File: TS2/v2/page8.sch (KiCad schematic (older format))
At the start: 16 parts, among them SW4 ABORT, U28 74LS148, U32 74LS138, U33 74LS138, U34 74LS00, U35 74LS74, U4 74LS06

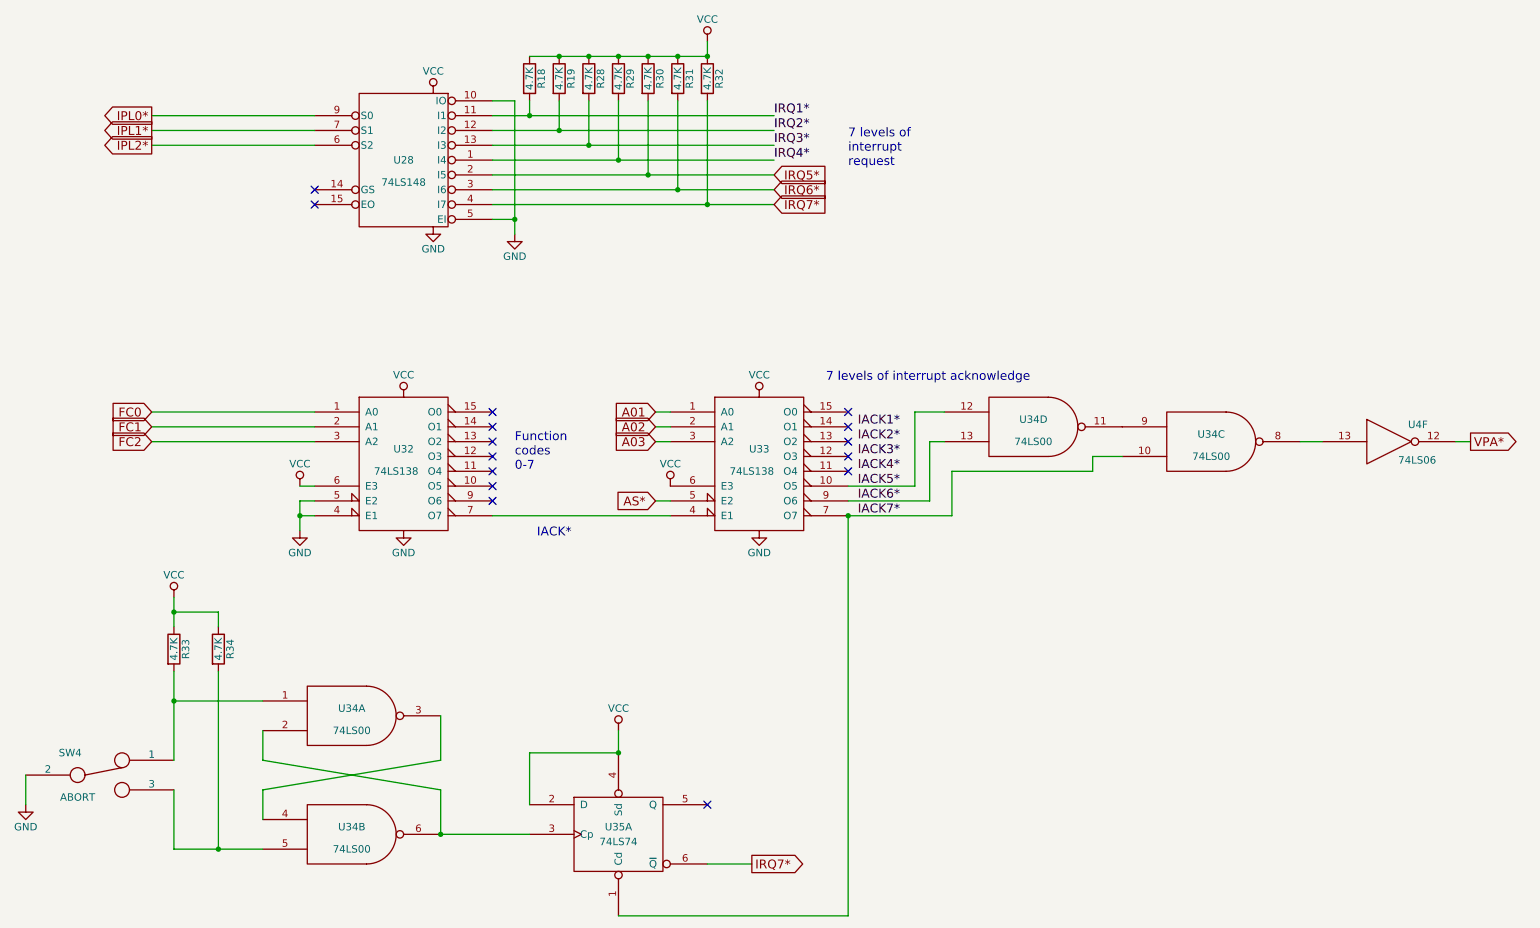
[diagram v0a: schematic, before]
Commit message: Corrections to interrupt circuitry.
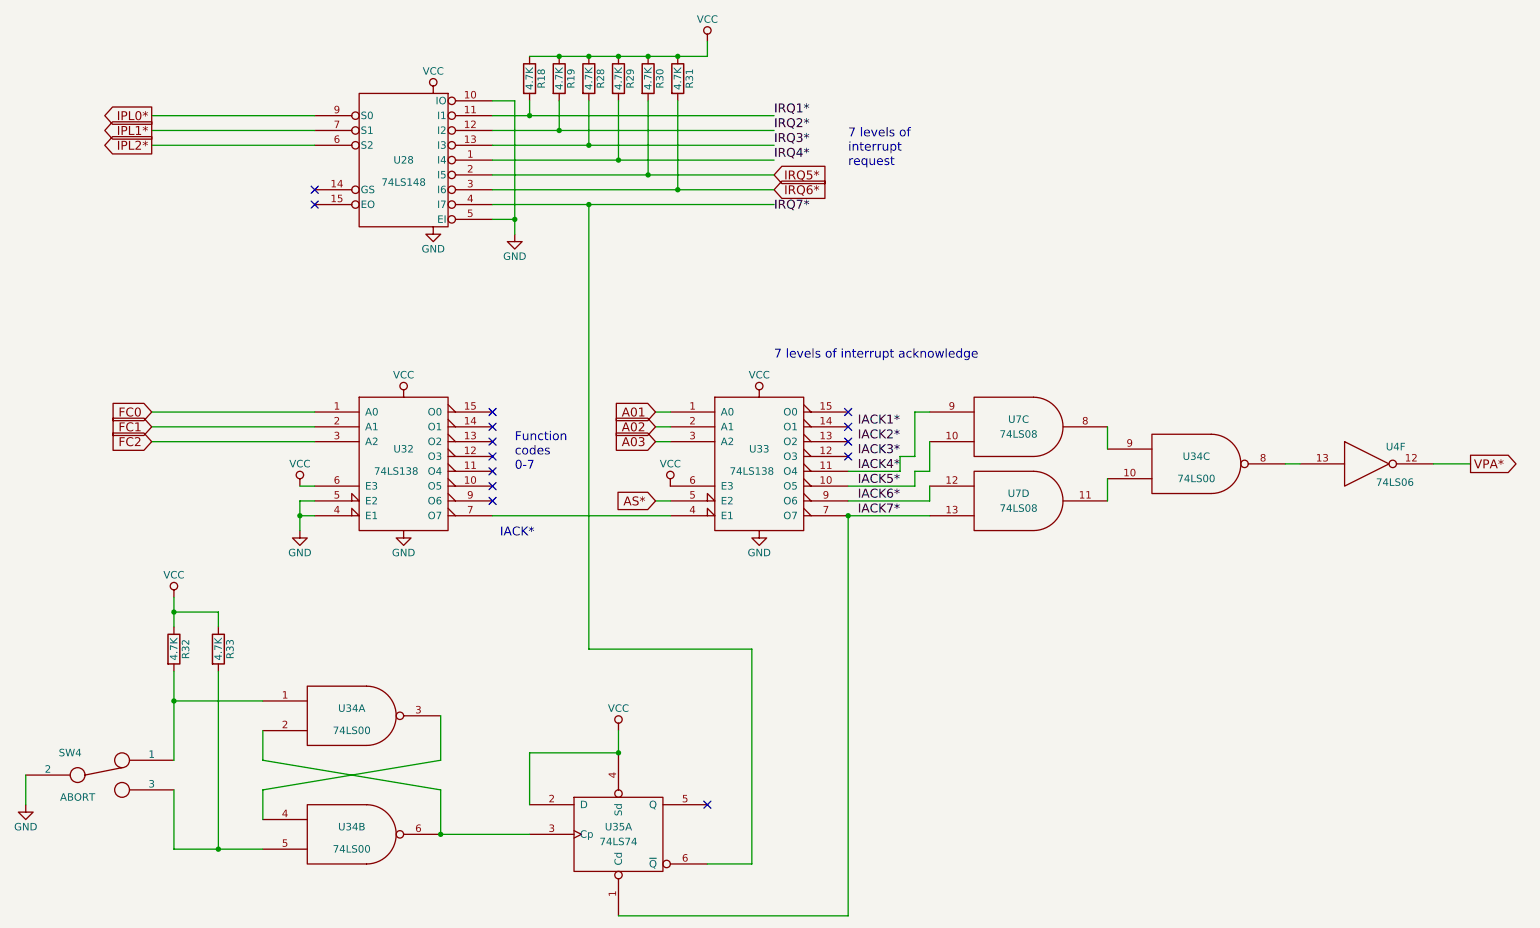
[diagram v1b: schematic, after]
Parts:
- removed R32: 4.7K, symbol R
- removed unit 4 of U34
- added U7: 74LS08, symbol 74LS08
- renumbered R33 to R32, R34 to R33
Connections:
- net GND: now also U7.7 (GND), U7.7 (GND)
- net IACK3*: now also U33.11 (O4), U7.9
- net IACK5*: now also U7.10
- net IACK6*: now also U7.12
- net IACK7*: now also U7.13; no longer U34.10
- net IRQ7*: no longer U28.4 (I7), U35.6 (~Q)
- net VCC: now also U7.14 (VCC), U7.14 (VCC)
- net at U34.9: now also U7.8
- new net: U28.4 (I7), U35.6 (~Q)
- new net: U34.10, U7.11
- no-connect marks 15 -> 14
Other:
- moved on the sheet: U34C, U4F

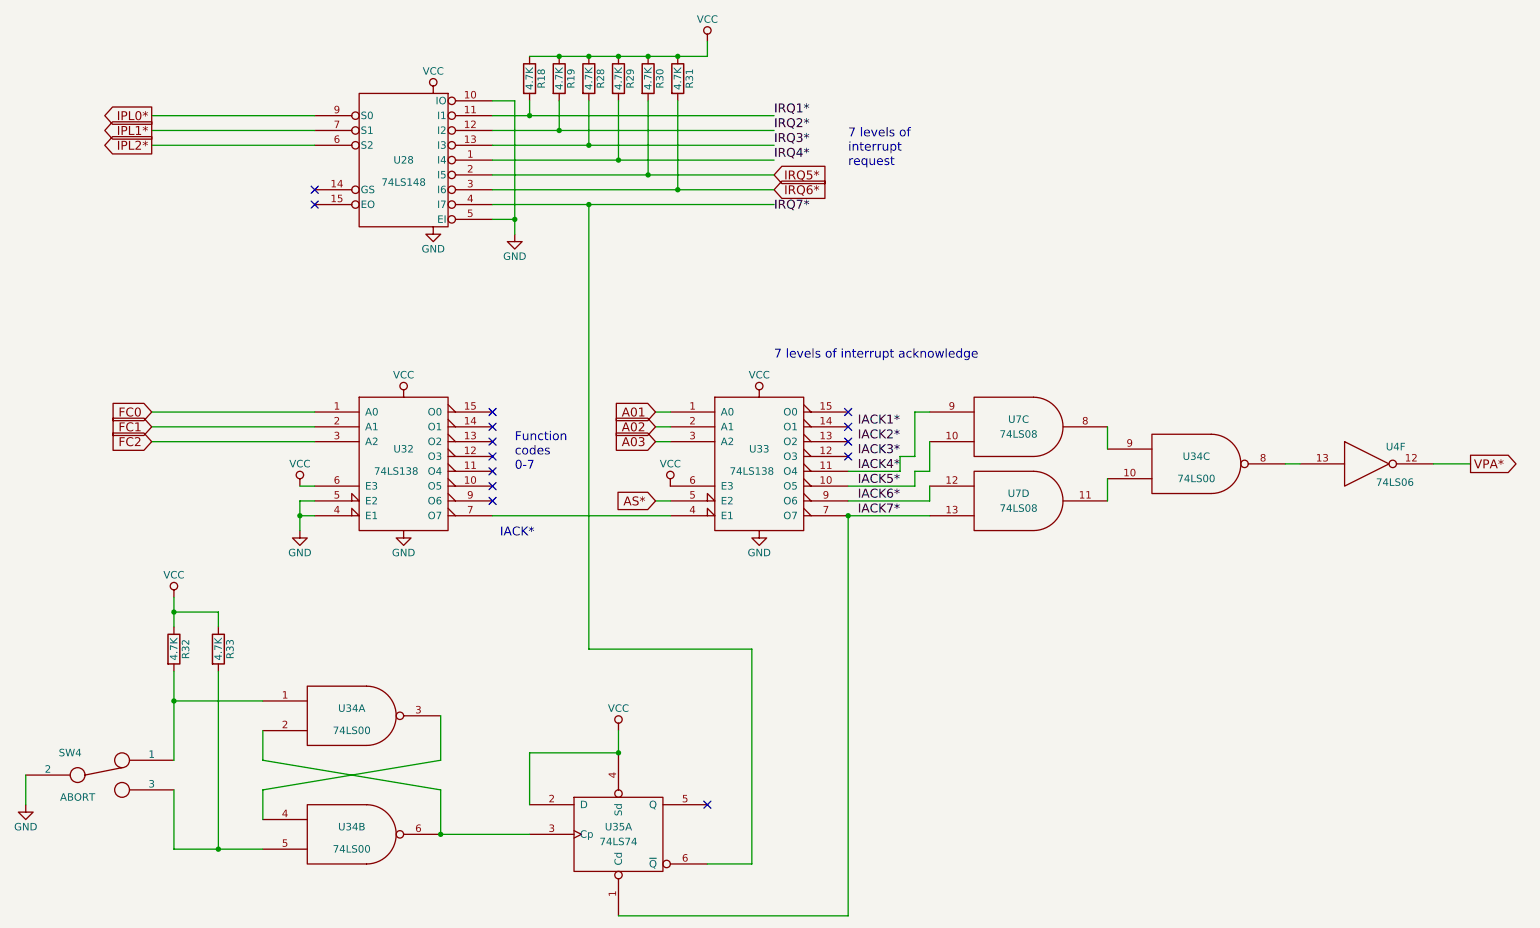
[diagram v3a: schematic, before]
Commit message: Add all bypass caps, show pullups as SIP resistors, start PCB layout.
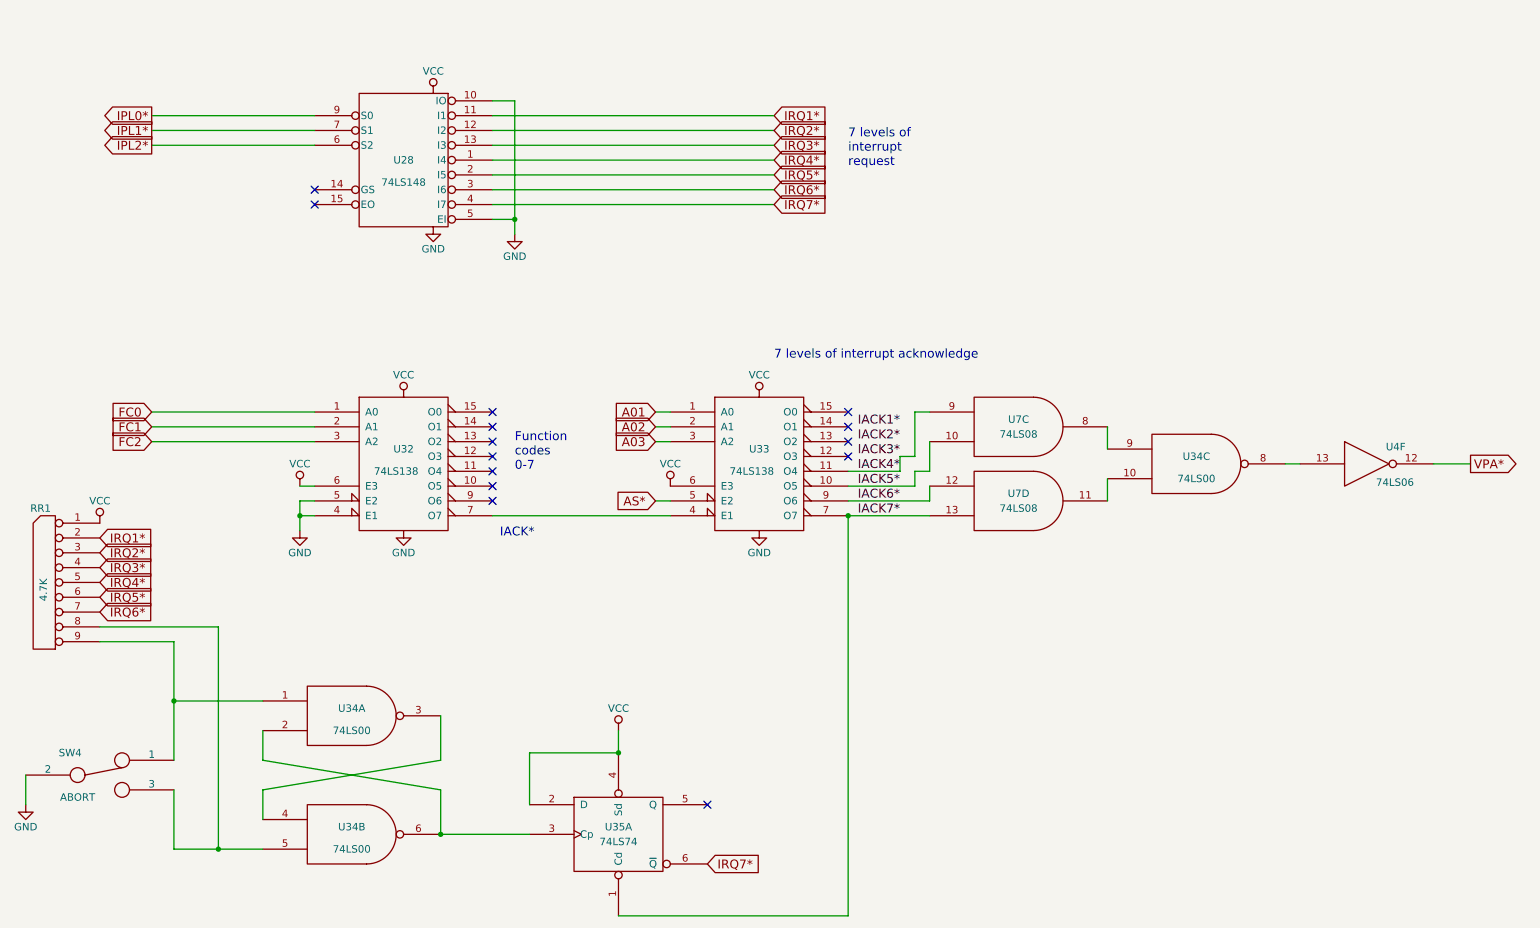
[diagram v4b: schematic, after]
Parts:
- removed R18, R19, R28, R29, R30, R31, R32, R33: 4.7K, symbol R
- added RR1: 4.7K, Resistors_ThroughHole:Resistor_Array_SIP8, symbol RR8
- SW4: footprint (none) -> Connect:PINHEAD1-3
- U28, U32, U33: footprint (none) -> Housings_DIP:DIP-16_W7.62mm
- U34, U35, U4, U7: footprint (none) -> Housings_DIP:DIP-14_W7.62mm
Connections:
- net IRQ1*: now also RR1.2
- net IRQ2*: now also RR1.3
- net IRQ3*: now also RR1.4
- net IRQ4*: now also RR1.5
- net IRQ5*: now also RR1.6
- net IRQ6*: now also RR1.7
- net IRQ7*: now also U28.4 (I7), U35.6 (~Q)
- net VCC: now also RR1.1 (COM)
- net at SW4.1, U34.1: now also RR1.9
- net at SW4.3, U34.5: now also RR1.8
